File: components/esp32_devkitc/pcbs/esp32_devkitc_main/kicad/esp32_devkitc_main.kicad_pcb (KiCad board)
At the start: 2 copper layers, 65 x 56 mm, 23 parts, among them J1 Conn_02x05_Odd_Even, J2 Conn_02x04_Odd_Even, J3 Conn_01x03_Male, P1 Conn_02x20_Odd_Even, U1 ESP32-DEVKITC-32D

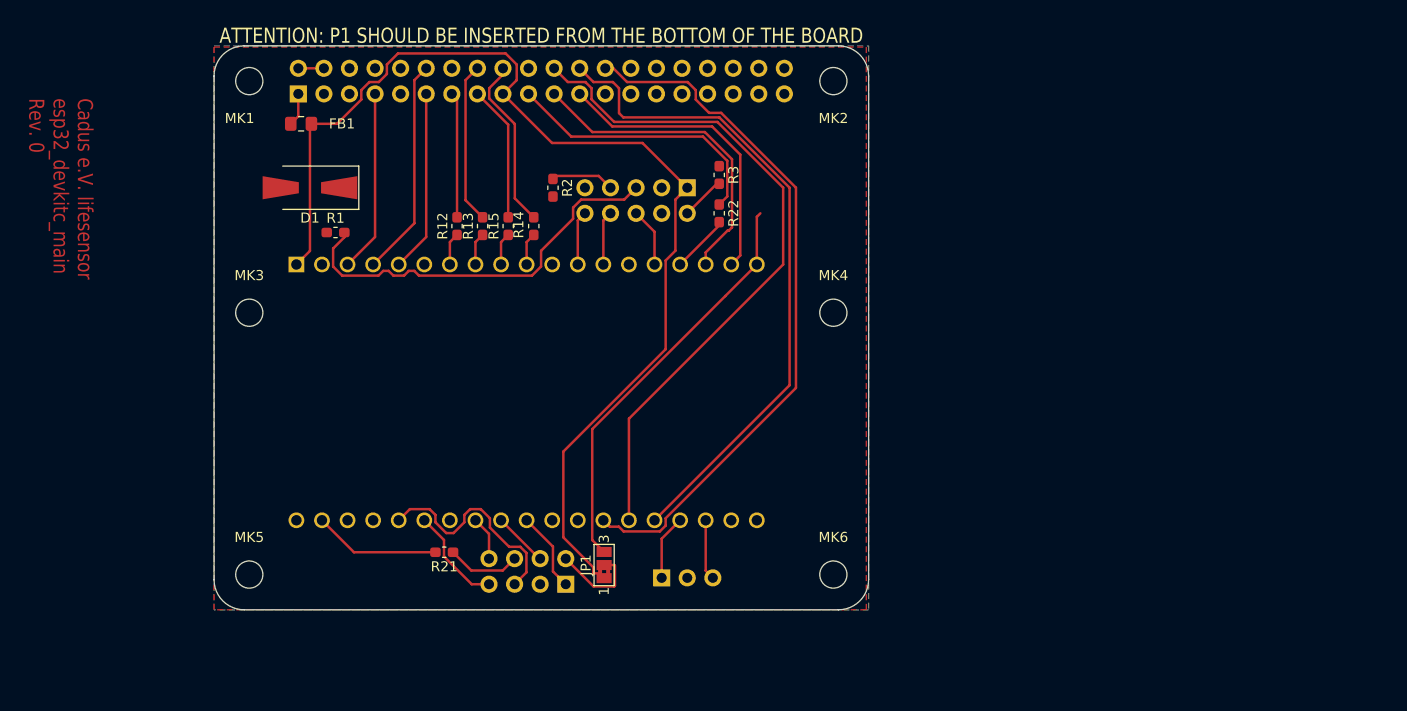
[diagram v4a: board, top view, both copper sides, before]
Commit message: first drafted routing, WARNING: JTAG TCK missing!
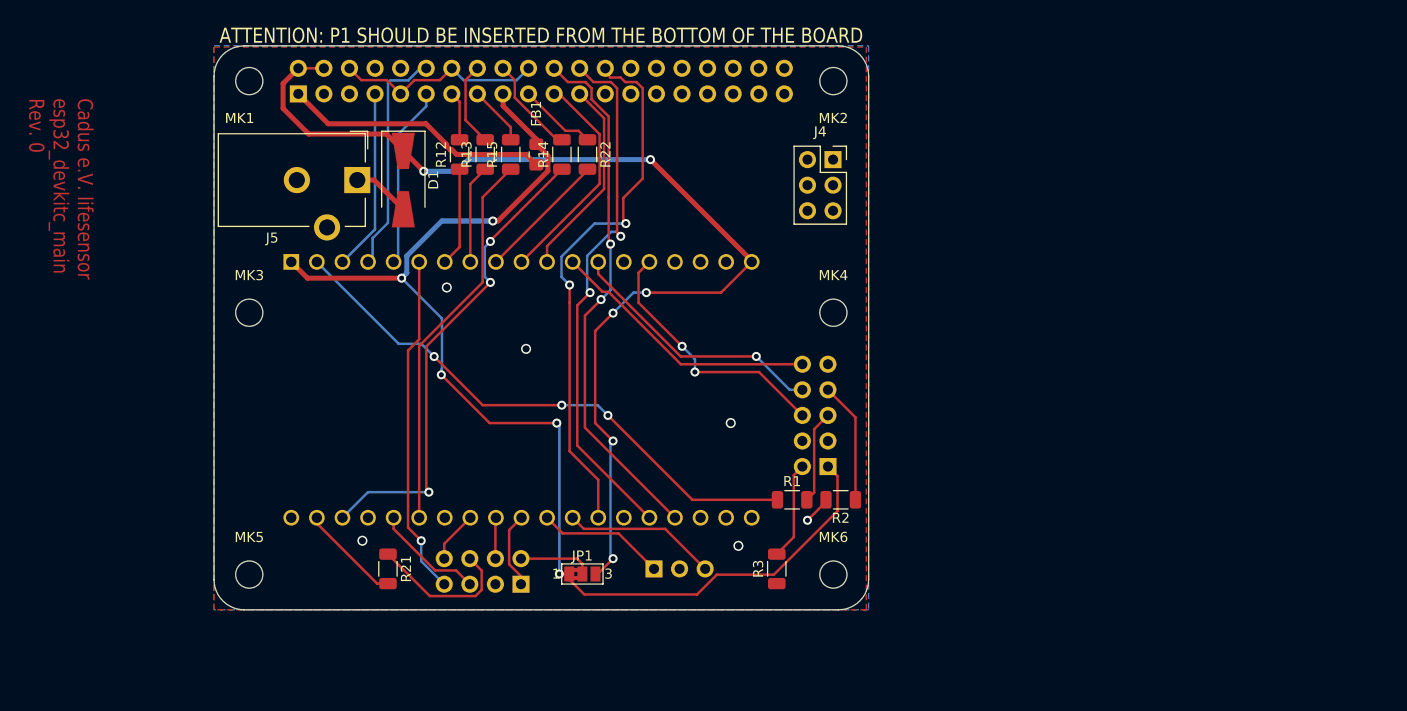
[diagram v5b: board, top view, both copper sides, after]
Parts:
- added J4: Conn_02x05_Odd_Even, Connector_PinSocket_2.54mm:PinSocket_2x03_P2.54mm_Vertical, F.Cu at (261.5, 105.3)
- added J5: Conn_01x02, Connector_BarrelJack:BarrelJack_CUI_PJ-102AH_Horizontal, F.Cu at (214.2, 107.3)
- R1, R12, R13, R14, R15, R2, R21, R22, R3: footprint Resistor_SMD:R_0603_1608Metric_Pad1.05x0.95mm_HandSolder -> Resistor_SMD:R_1206_3216Metric
- moved R1 52.5 mm to (257.4, 139.1)
- moved R2 42.2 mm to (262.2, 139.1), turned to 180 degrees
- moved R3 39.5 mm to (255.9, 145.9), turned to 90 degrees
- moved J1 31.0 mm to (261.0, 135.8), turned to 0 degrees
- moved FB1 23.6 mm to (232.0, 104.8), turned to 270 degrees
- moved R22 14.3 mm to (237.1, 104.8)
- moved D1 9.30 mm to (218.8, 107.3), turned to 270 degrees
- moved R14 7.64 mm to (234.5, 104.8)
- moved R13 7.12 mm to (226.9, 104.8)
- moved R12 7.12 mm to (224.4, 104.8)
- moved R15 7.12 mm to (229.5, 104.8)
- moved R21 5.83 mm to (217.3, 145.9), turned to 270 degrees
- moved J2 4.45 mm to (230.5, 147.5)
- moved JP1 2.33 mm to (236.6, 146.4), turned to 0 degrees
- moved J3 1.17 mm to (243.7, 145.9)
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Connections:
- U1 pad 10: Net-(R14-Pad1) -> /SENS_MISO
- U1 pad 11: Net-(U1-Pad11) -> /SENS_SCLK
- U1 pad 16: Net-(R22-Pad2) -> Net-(U1-Pad16)
- U1 pad 17: /SENS_MISO -> Net-(U1-Pad17)
- U1 pad 18: /SENS_SCLK -> Net-(U1-Pad18)
- U1 pad 22: Net-(U1-Pad22) -> Net-(R14-Pad1)
- U1 pad 25: /DISP_INT_TOUCH -> Net-(R15-Pad1)
- U1 pad 30: Net-(U1-Pad30) -> /PROC_SDA
- U1 pad 31: Net-(U1-Pad31) -> /PROC_SCL
- U1 pad 33: /~SENS_CS_BPM -> Net-(U1-Pad33)
- U1 pad 35: /PROC_SDA -> /~SENS_CS_BPM
- U1 pad 36: /PROC_SCL -> Net-(U1-Pad36)
- U1 pad 6: Net-(U1-Pad6) -> /DISP_INT_TOUCH
- U1 pad 9: Net-(R15-Pad1) -> Net-(R22-Pad2)
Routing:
- net /SENS_5V_ANA: track 43.6 -> 105.3 mm, vias 0 -> 6
- net /JTAG_~TRST: track 0.00 -> 55.5 mm, vias 0 -> 3
- net Net-(R14-Pad1): track 3.23 -> 47.9 mm, vias 0 -> 3
- net Net-(R15-Pad1): track 3.23 -> 38.4 mm
- net Net-(J1-Pad5): track 40.3 -> 9.25 mm
- net /DISP_INT_TOUCH: track 10.0 -> 33.9 mm, vias 0 -> 1
- net GND: track 0.00 -> 23.7 mm, vias 0 -> 6
- net /SENS_3V3_ANA: track 3.28 -> 26.7 mm
- net /JTAG_TMS: track 5.37 -> 27.0 mm
- net /JTAG_TDI: track 5.37 -> 26.2 mm, vias 0 -> 1
- net /JTAG_TDO: track 5.84 -> 26.2 mm, vias 0 -> 2
- net /SENS_MOSI: track 27.2 -> 7.74 mm
- net /~SENS_CS_SPO2: track 70.2 -> 54.3 mm, vias 0 -> 2
- net /~SENS_CS_BPM: track 67.7 -> 53.4 mm, vias 0 -> 2
- net /~SENS_CS_ECG: track 65.8 -> 53.5 mm, vias 0 -> 2
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
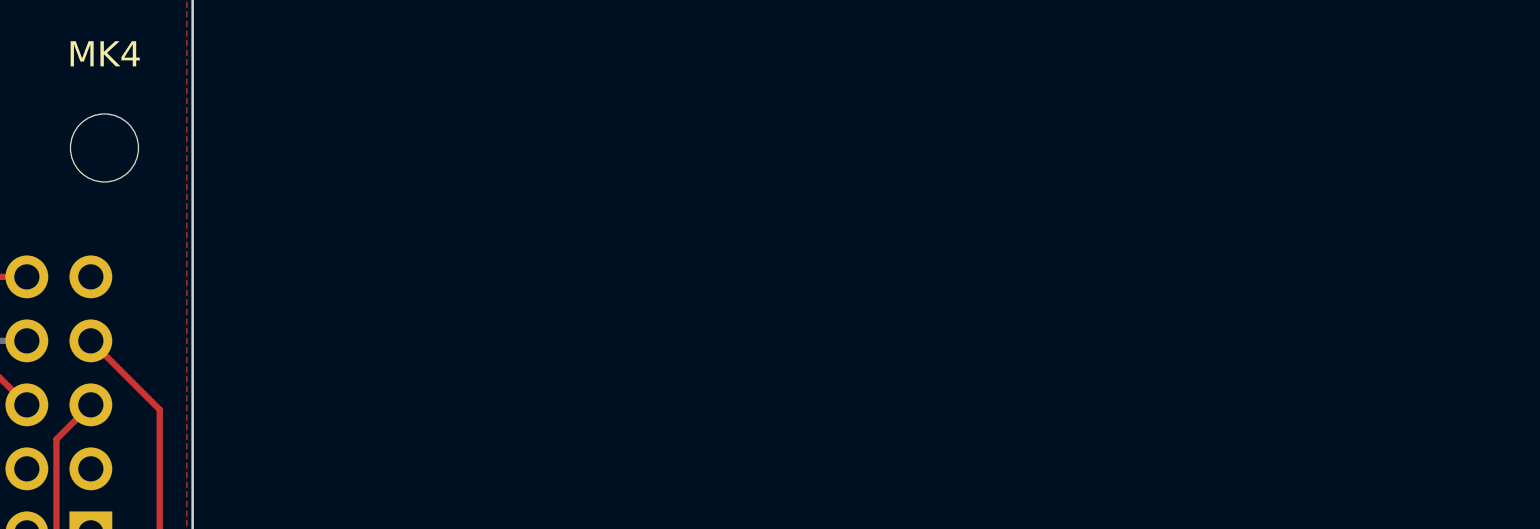
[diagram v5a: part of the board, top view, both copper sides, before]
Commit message: adds todos and notes
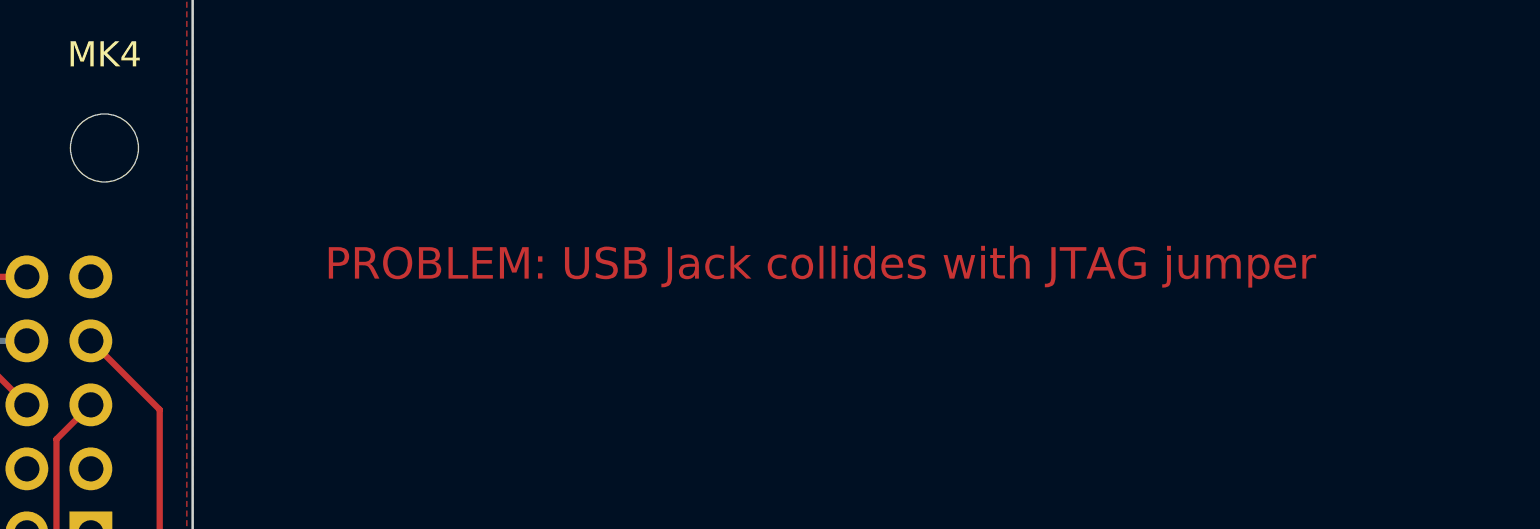
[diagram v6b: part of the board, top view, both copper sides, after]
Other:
- board text added: "PROBLEM: USB Jack collides with JTAG jumper"

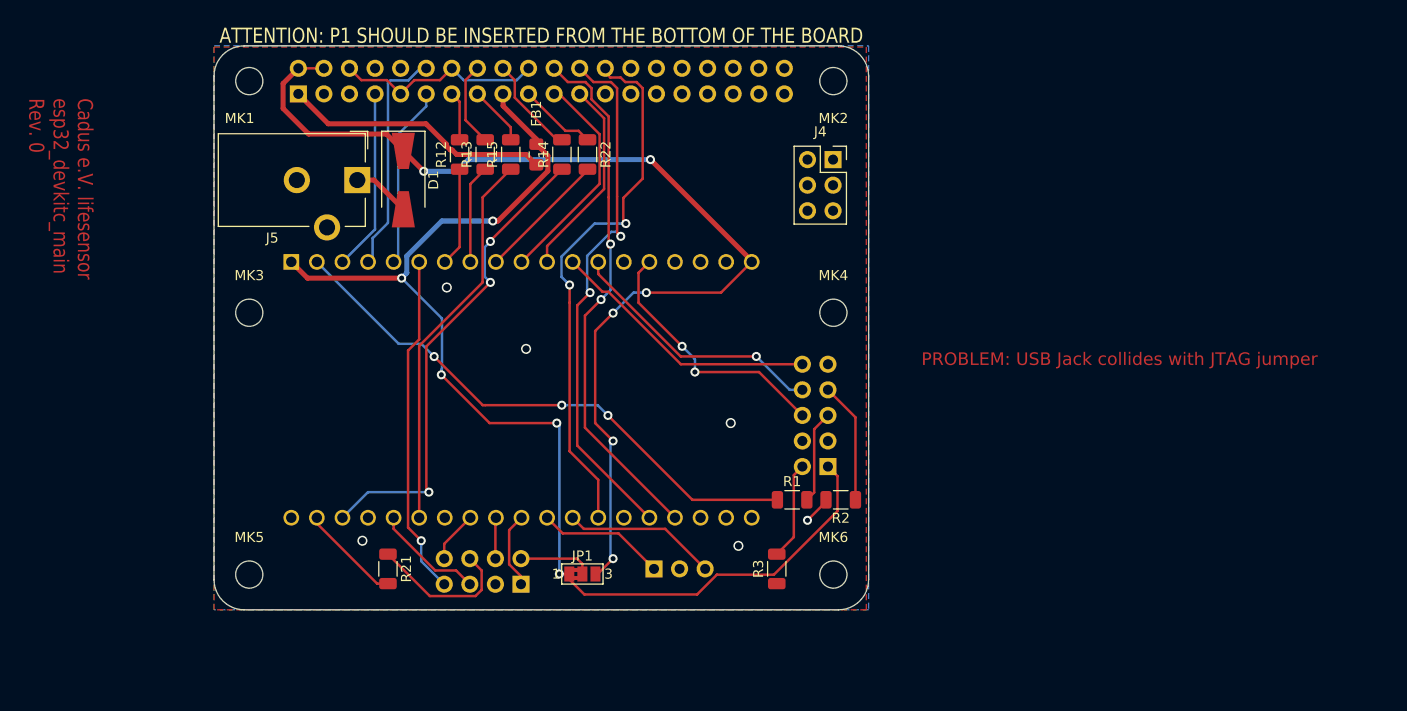
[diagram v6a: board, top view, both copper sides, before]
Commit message: Ready for review! fixes JTAG, adds updated pinout, updates JTAG header docu in Development_esp32_devkitc, finishes routing, adds JTAG resistors according to ESP32 manual
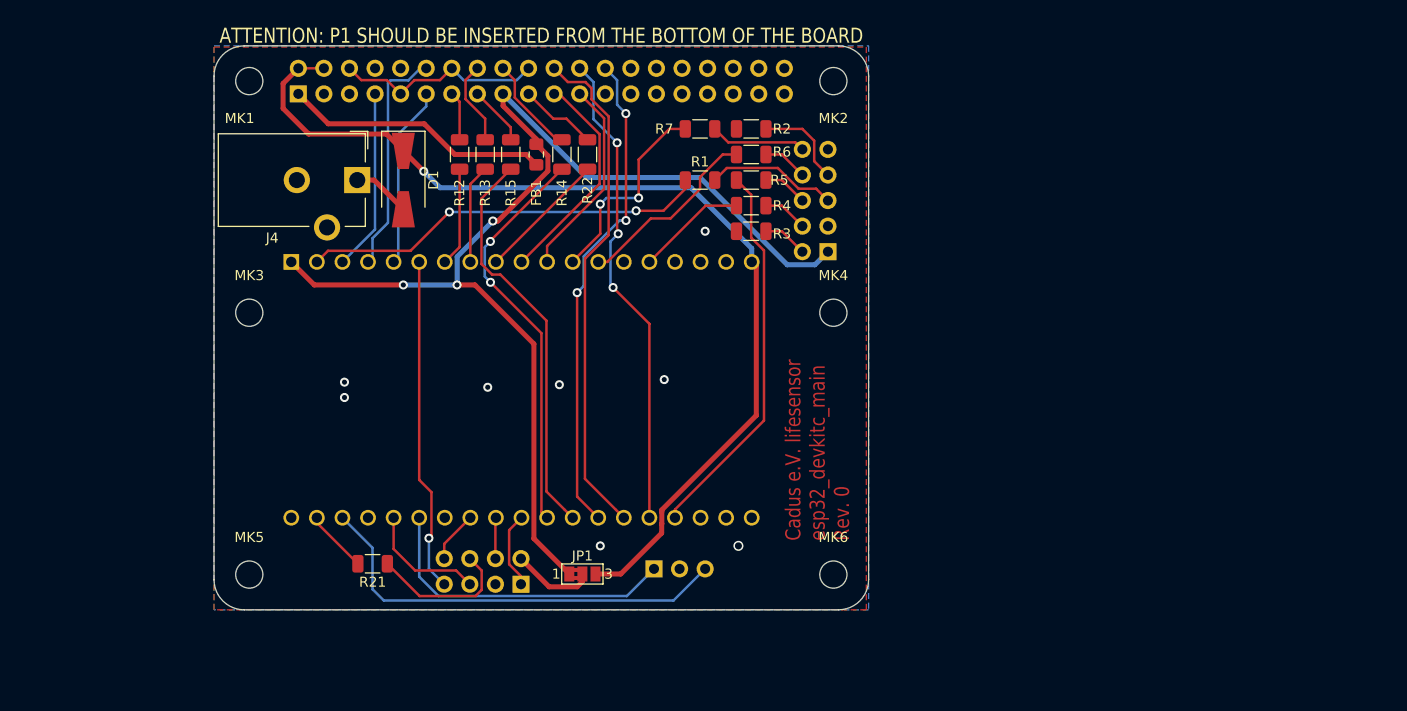
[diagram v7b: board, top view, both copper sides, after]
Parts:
- removed the J4 at (261.5, 105.3)
- added R4: 100, Resistor_SMD:R_1206_3216Metric, F.Cu at (253.3, 109.9)
- added R5: 100, Resistor_SMD:R_1206_3216Metric, F.Cu at (253.3, 107.3)
- added R6: 100, Resistor_SMD:R_1206_3216Metric, F.Cu at (253.3, 104.8)
- added R7: 100, Resistor_SMD:R_1206_3216Metric, F.Cu at (248.3, 102.2)
- moved R2 37.9 mm to (253.3, 102.2)
- moved R3 33.6 mm to (253.3, 112.4), turned to 0 degrees
- moved R1 33.0 mm to (248.3, 107.3)
- moved J1 21.3 mm to (261.0, 114.4)
- moved R21 1.61 mm to (215.7, 145.4), turned to 180 degrees
- renumbered J5 to J4
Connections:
- J1 pad 10: /JTAG_TMS -> Net-(J1-Pad10)
- J1 pad 4: /JTAG_TCK -> Net-(J1-Pad4)
- J1 pad 6: /JTAG_TDO -> Net-(J1-Pad6)
- J1 pad 8: /JTAG_TDI -> Net-(J1-Pad8)
- U1 pad 15: /JTAG_TDO -> /JTAG_TCK
- U1 pad 22: Net-(R14-Pad1) -> /PROC_SCL
- U1 pad 25: Net-(R15-Pad1) -> /PROC_SDA
- U1 pad 30: /PROC_SDA -> Net-(R14-Pad1)
- U1 pad 31: /PROC_SCL -> Net-(R15-Pad1)
- U1 pad 33: Net-(U1-Pad33) -> /~SENS_CS_BPM
- U1 pad 35: /~SENS_CS_BPM -> /JTAG_TDO
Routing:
- net /PROC_SCL: track 15.3 -> 43.1 mm
- net /PROC_SDA: track 12.7 -> 31.1 mm
- net /JTAG_~TRST: track 55.5 -> 40.5 mm, vias 3 -> 2
- net /JTAG_TDO: track 26.2 -> 38.3 mm, vias 2 -> 0
- net /JTAG_TCK: track 0.00 -> 11.0 mm
- net Net-(J1-Pad10): track 0.00 -> 9.54 mm
- net Net-(R14-Pad1): track 47.9 -> 40.3 mm, vias 3 -> 2
- net /JTAG_TDI: track 26.2 -> 18.8 mm, vias 1 -> 0
- net /JTAG_TMS: track 27.0 -> 20.6 mm, vias 0 -> 2
- net /~SENS_CS_SPO2: track 54.3 -> 48.7 mm, vias 2 -> 3
- net /~SENS_CS_ECG: track 53.5 -> 48.1 mm, vias 2 -> 3
- net /JTAG_RTCK: track 9.75 -> 4.46 mm
- net /SENS_5V_ANA: track 105.3 -> 100.1 mm, vias 6 -> 1
- net Net-(J1-Pad4): track 0.00 -> 4.46 mm
- net Net-(J1-Pad8): track 0.00 -> 4.46 mm
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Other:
- board text added: "USB JACK"
- board text removed: "PROBLEM: USB Jack collides with JTAG jumper"

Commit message: small cleanup
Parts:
- moved FB1 1.14 mm to (231.0, 104.3)
- moved R13 1.02 mm to (225.9, 104.8)
- moved R12 1.02 mm to (223.4, 104.8)
- moved R15 1.02 mm to (228.4, 104.8)
- moved R14 0.76 mm to (233.8, 104.8)
- moved R22 0.76 mm to (236.3, 104.8)
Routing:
- net /SENS_3V3_DIG: track 116.5 -> 109.4 mm
- net GND: track 20.9 -> 27.0 mm, vias 8 -> 7
- net /JTAG_TMS: track 20.6 -> 18.4 mm, vias 2 -> 0
- net /~SENS_CS_SPO2: track 48.7 -> 50.7 mm
- net Net-(R14-Pad1): track 40.3 -> 38.4 mm
- net /~SENS_CS_BPM: track 50.5 -> 52.3 mm
- net /JTAG_TDI: track 18.8 -> 20.2 mm
- net /SENS_3V3_ANA: track 26.6 -> 25.3 mm
- net /SENS_MOSI: track 7.74 -> 6.79 mm
- net Net-(R15-Pad1): track 40.0 -> 39.1 mm
- net /SENS_MISO: track 22.1 -> 21.3 mm
- net /~SENS_CS_ECG: track 48.1 -> 47.5 mm
- net Net-(R22-Pad2): track 13.0 -> 12.3 mm
- net /JTAG_~TRST: track 40.5 -> 40.0 mm
- net /DISP_INT_TOUCH: track 33.2 -> 33.5 mm, vias 1 -> 2
